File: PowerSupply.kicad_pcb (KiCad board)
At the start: 2 copper layers, 105 x 200 mm, 32 parts, among them J1 Barrel_Jack, J2 Conn_02x06_Odd_Even, M1 MouseBites, M2 MouseBites, M3 MouseBites, M4 MouseBites, SW1 SW_SPST, U1 LM7805_TO220, U2 LM7812_TO220, U3 LM7912_TO220

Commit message: layout started
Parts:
- added D7: 12V LED, LED_THT:LED_D5.0mm, F.Cu at (165.0, 120.0)
- added D8: -12V LED, LED_THT:LED_D5.0mm, F.Cu at (165.0, 150.0)
- added H2: MountingHole, MountingHole:MountingHole_3.2mm_M3, F.Cu at (110.0, 70.0)
- added H3: MountingHole, MountingHole:MountingHole_3.2mm_M3, F.Cu at (165.0, 210.0)
- added H4: MountingHole, MountingHole:MountingHole_3.2mm_M3, F.Cu at (165.0, 70.0)
- added H5: MountingHole, MountingHole:MountingHole_3.2mm_M3, F.Cu at (110.0, 210.0)
- added H7: LEDMount, MountingHole:MountingHole_5mm, F.Cu at (110.0, 119.0)
- added H8: LEDMount, MountingHole:MountingHole_5mm, F.Cu at (110.0, 134.0)
- added R2: 150R, Resistor_SMD:R_0805_2012Metric_Pad1.20x1.40mm_HandSolder, F.Cu at (165.0, 112.5)
- added R3: 150R, Resistor_SMD:R_0805_2012Metric_Pad1.20x1.40mm_HandSolder, F.Cu at (165.0, 142.5)
- C2, C3, C4, D3, D4, J1, U1, U2: moved to B.Cu
- D6: value LED -> 5V LED; footprint Connector_Wire:SolderWire-1sqmm_1x02_P5.4mm_D1.4mm_OD2.7mm_Relief -> LED_THT:LED_D5.0mm
- H6: renamed from H1; footprint Synth:PowerLEDMount -> MountingHole:MountingHole_5mm
- J2: footprint Connector_IDC:IDC-Header_2x06_P2.54mm_Vertical -> Synth:IDC-Header_2x06_P2.54mm_Vertical; moved to B.Cu
- moved C2 330.6 mm to (172.8, 142.5)
- moved C4 327.6 mm to (172.8, 167.5), turned to 0 degrees
- moved D3 185.7 mm to (145.0, 86.3), turned to 90 degrees
- moved U1 181.1 mm to (152.5, 82.5), turned to 90 degrees
- moved C6 154.1 mm to (149.0, 121.0), turned to 90 degrees
- moved C3 146.2 mm to (147.8, 142.5)
- moved D4 140.2 mm to (145.0, 126.3), turned to 90 degrees
- moved U2 135.1 mm to (152.5, 122.5), turned to 90 degrees
- moved C1 125.3 mm to (147.8, 167.5), turned to 0 degrees
- moved C5 122.9 mm to (149.0, 81.0), turned to 90 degrees
- moved C7 100.1 mm to (308.0, 182.0), turned to 180 degrees
- moved C9 86.2 mm to (360.0, 197.0)
- moved R1 85.0 mm to (165.0, 127.5)
- moved C12 73.0 mm to (362.4, 188.0)
- moved C11 71.6 mm to (340.0, 125.0)
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- renumbered H2 to H1
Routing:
- added copper zone on F.Cu, net GND

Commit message: Gerbers sent for production
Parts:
- added G***: LOGO, Graphics:lightning, F.Cu at (143.0, 139.8)
- added G***: LOGO, Graphics:lightning2, F.Cu at (113.9, 199.8)
- added G***: LOGO, Graphics:elecwarning, F.Cu at (110.0, 66.0)
- added G***: LOGO, Graphics:lightning, B.Cu at (168.4, 147.1)
- added kibuzzard-61F37152: G***, kibuzzard-61F37152, F.Cu at (110.0, 114.0)
- added kibuzzard-61F37174: G***, kibuzzard-61F37174, F.Cu at (110.0, 144.0)
- added kibuzzard-61F37DAA: G***, kibuzzard-61F37DAA, F.Cu at (110.0, 129.0)
- C11, C12, C13, D1, D2, D5, U3: moved to B.Cu
- moved C9 229.4 mm to (149.0, 107.0), turned to 180 degrees
- moved C12 227.1 mm to (151.4, 104.0)
- moved C8 203.8 mm to (149.0, 72.0)
- moved C11 197.1 mm to (151.4, 68.0), turned to 180 degrees
- moved C10 192.9 mm to (181.0, 107.0)
- moved C13 186.3 mm to (183.4, 104.0), turned to 180 degrees
- moved U3 148.4 mm to (177.9, 117.5), turned to -90 degrees
- moved D5 143.9 mm to (185.0, 113.7), turned to -90 degrees
- moved C7 140.9 mm to (181.0, 121.0), turned to 90 degrees
- moved J2 18.8 mm to (179.0, 77.5)
- moved U1 6.02 mm to (152.1, 88.5)
- moved C5 6.00 mm to (149.0, 87.0)
- moved D3 6.00 mm to (145.0, 92.3)
- moved U2 0.45 mm to (152.1, 122.5)
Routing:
- net +5V: track 0.00 -> 138.2 mm, vias 0 -> 3
- net Net-(C1-Pad1): track 0.00 -> 114.9 mm
- net +12V: track 0.00 -> 94.5 mm
- net -12V: track 0.00 -> 93.2 mm
- net Net-(C2-Pad2): track 0.00 -> 69.5 mm
- net Net-(D1-Pad2): track 0.00 -> 22.6 mm
- net Net-(J1-Pad1): track 0.00 -> 16.1 mm
- net Net-(D8-Pad2): track 0.00 -> 5.37 mm
- net Net-(D6-Pad2): track 0.00 -> 5.37 mm
- net Net-(D7-Pad2): track 0.00 -> 5.37 mm
- added copper zone on B.Cu, net GND

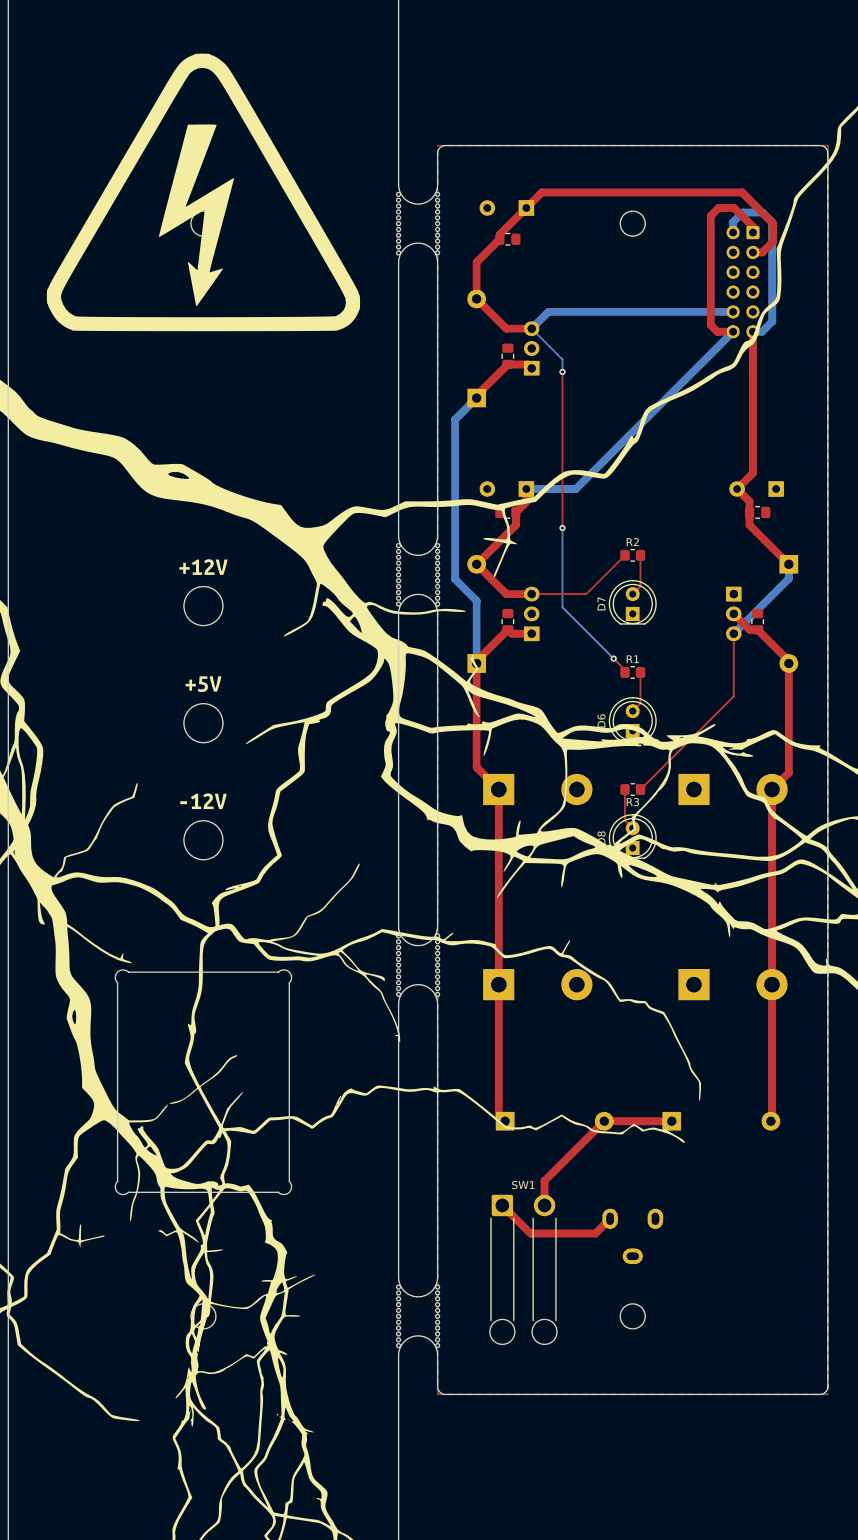
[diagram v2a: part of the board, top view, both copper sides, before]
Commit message: Add Moutning Holes
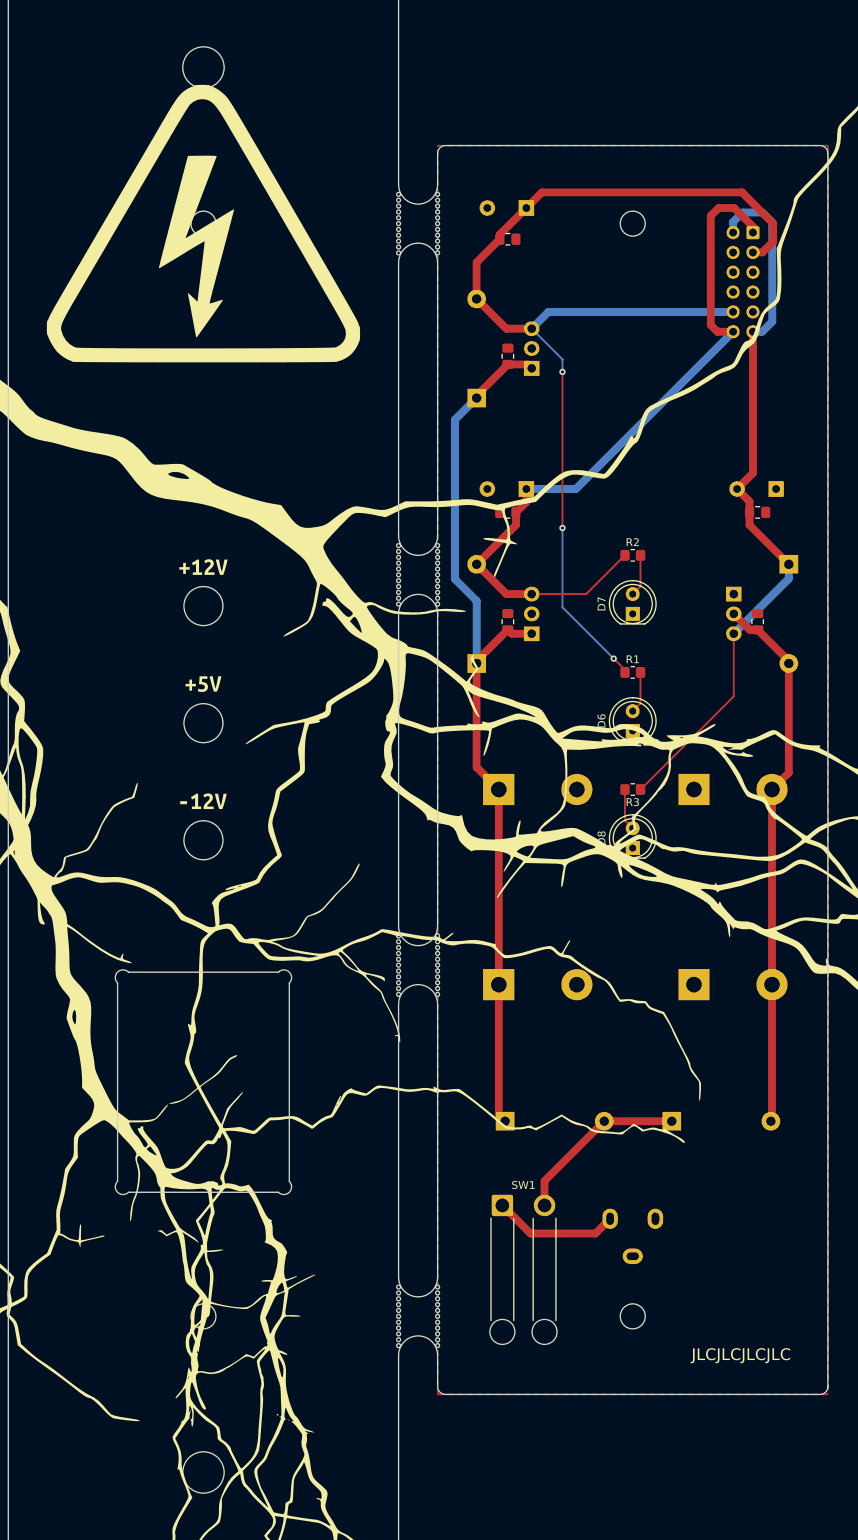
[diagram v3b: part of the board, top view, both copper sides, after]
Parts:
- added H10: MountingHole, MountingHole:MountingHole_5.3mm_M5, F.Cu at (110.0, 50.0)
- added H9: MountingHole, MountingHole:MountingHole_5.3mm_M5, F.Cu at (110.0, 230.0)
- moved G*** 4.00 mm to (110.0, 70.0)
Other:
- board text added: "JLCJLCJLCJLC"

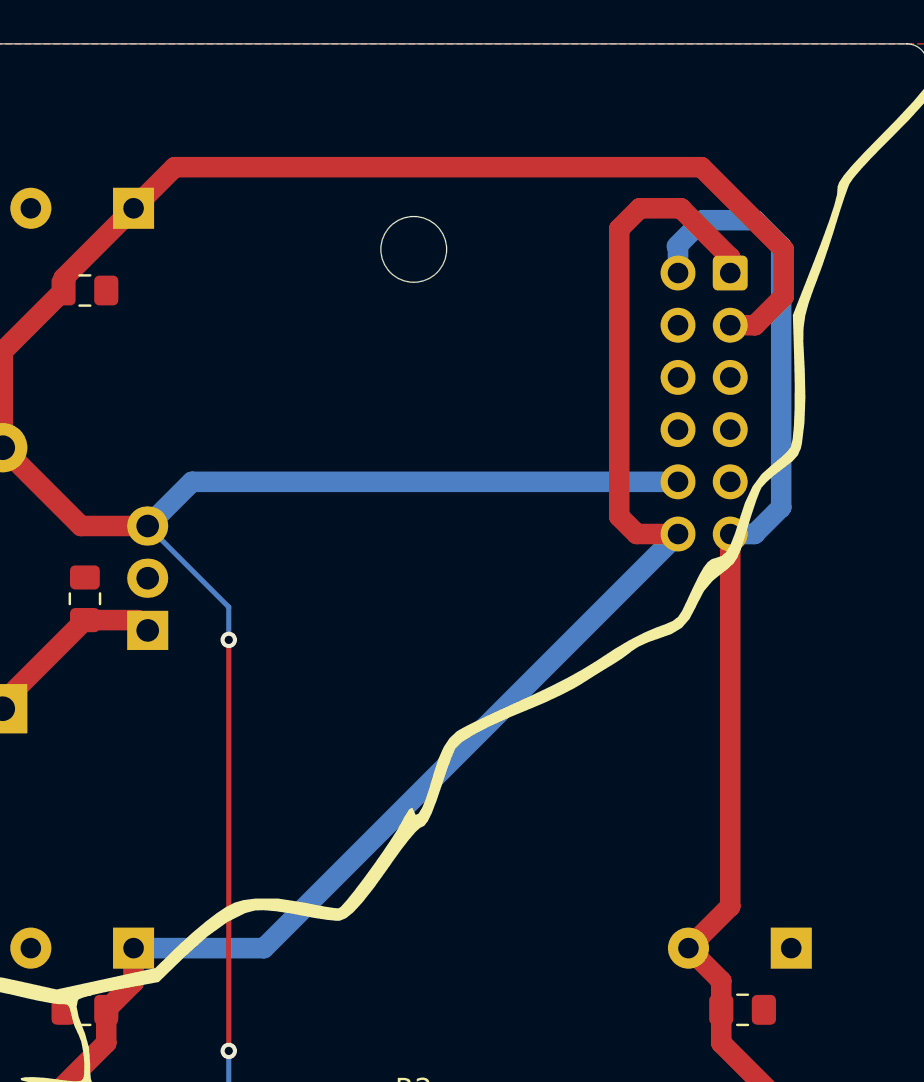
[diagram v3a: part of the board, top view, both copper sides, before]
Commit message: Changed IDC to 2x5
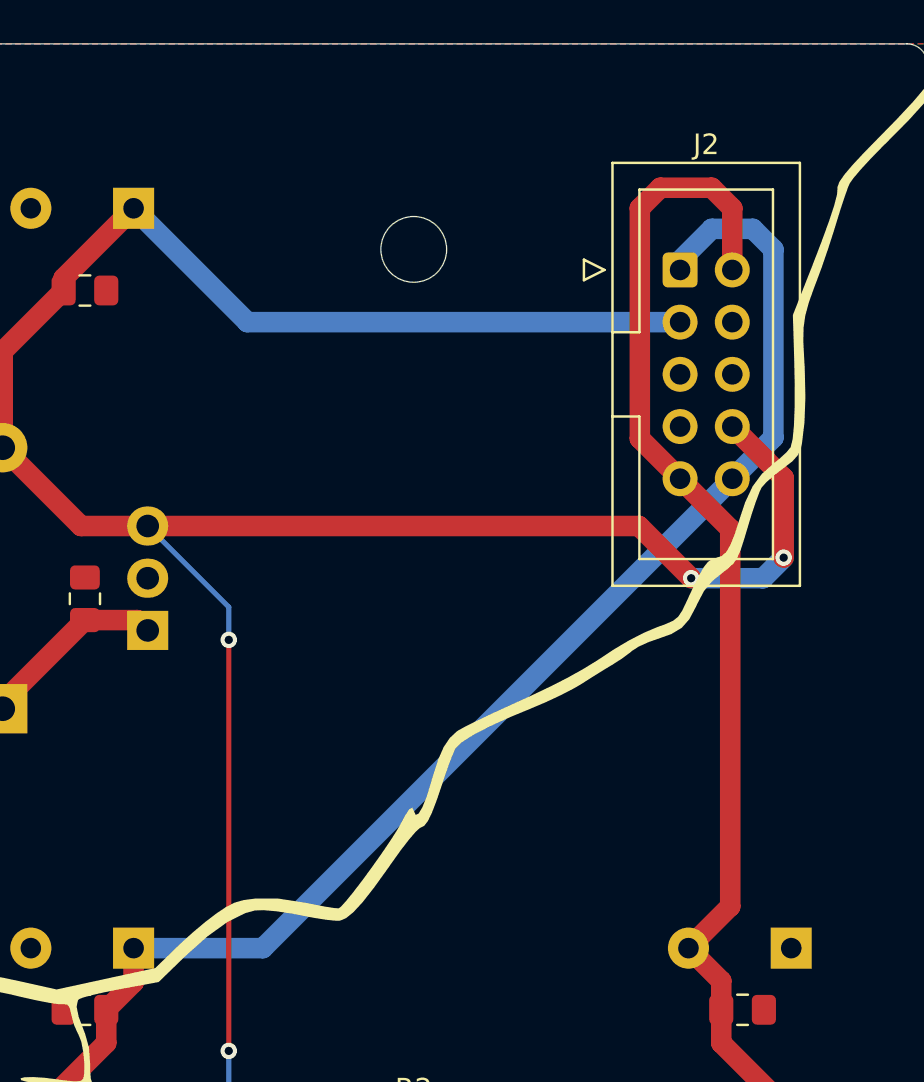
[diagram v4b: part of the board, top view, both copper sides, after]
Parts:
- J2: value Conn_02x06_Odd_Even -> PowerHeader; footprint Synth:IDC-Header_2x06_P2.54mm_Vertical -> Connector_IDC:IDC-Header_2x05_P2.54mm_Vertical; moved to F.Cu
- moved J2 6.58 mm to (178.0, 71.0), turned to 0 degrees
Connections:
- J2 pad 10: +5V -> +12V
- J2 pad 8: GND -> +5V
- J2 pad 9: GND -> -12V
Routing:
- net +12V: track 94.5 -> 91.6 mm
- net -12V: track 93.2 -> 96.1 mm
- net +5V: track 138.2 -> 140.6 mm, vias 3 -> 5
